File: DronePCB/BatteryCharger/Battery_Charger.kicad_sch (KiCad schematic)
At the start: 43 parts, among them Q1 AO3400A, Q2 AO3400A, Q3 SiS454DN, Q4 SiS454DN, Q5 AO3400A, U1 BQ24725A

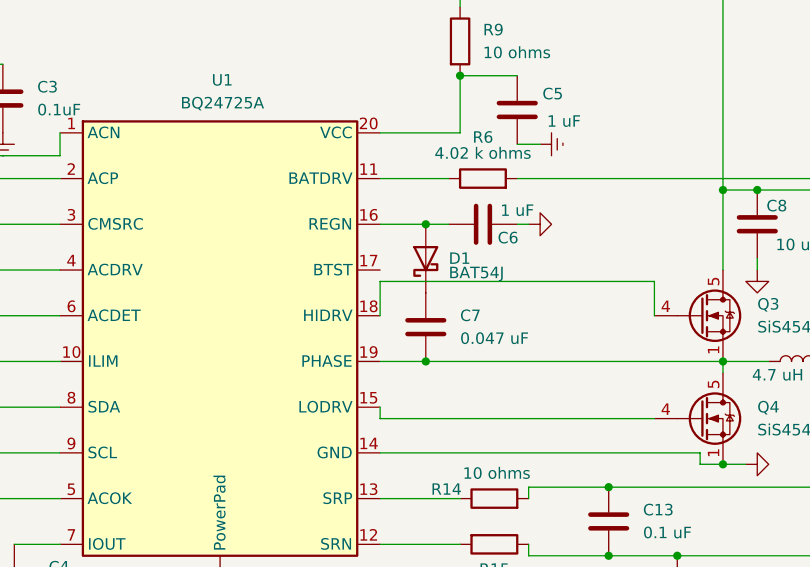
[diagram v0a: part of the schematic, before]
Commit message: Fixed a connection in battery circuit and updated project to KiCAD 10.0.0
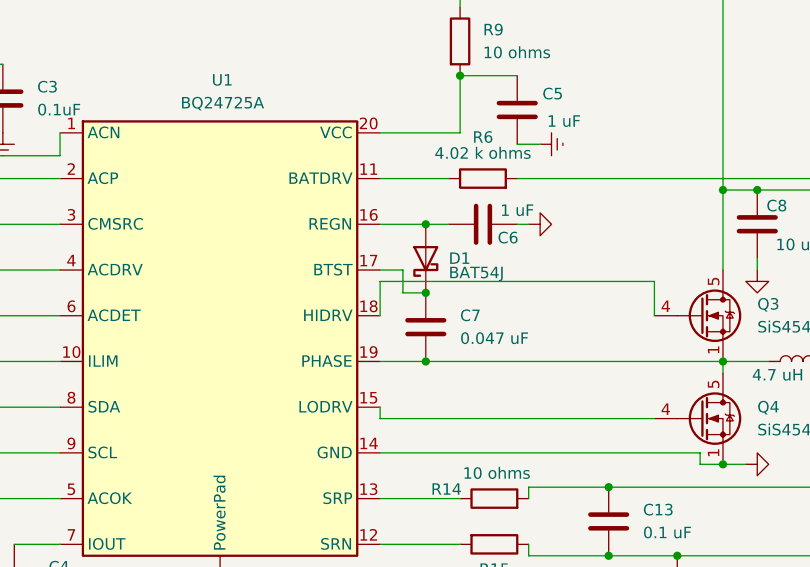
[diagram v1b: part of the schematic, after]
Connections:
- net at C7.1, D1.1 (K): now also U1.17 (BTST)
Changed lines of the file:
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@@
+	)
+	(junction
+		(at 124.46 60.96)
+		(diameter 0)
+		(color 0 0 0 0)
 	)
 	(junction
@@
 	(wire
 		(pts
+			(xy 121.92 58.42) (xy 121.92 60.96)
+		)
+		(stroke
+			(width 0)
+			(type default)
+		)
+	)
+	(wire
+		(pts
 			(xy 144.78 82.55) (xy 135.89 82.55)
 		)
@@
 	(wire
 		(pts
+			(xy 121.92 60.96) (xy 124.46 60.96)
+		)
+		(stroke
+			(width 0)
+			(type default)
+		)
+	)
+	(wire
+		(pts
 			(xy 62.23 68.58) (xy 64.77 68.58)
 		)
@@
 		)
 		(stroke
+			(width 0)
+			(type default)
+		)
+	)
+	(wire
+		(pts
+			(xy 119.38 58.42) (xy 121.92 58.42)
+		)
+		(stroke
